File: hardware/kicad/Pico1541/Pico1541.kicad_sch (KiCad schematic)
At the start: 36 parts, among them J1 SWD, J2 USB_A, J3 Micro SD Card, J4 DIN-6, J5 Serial, J6 Display/Keys, J7 OLED/Key_Hat, J8 OLED, J9 5V_EXT, Q1 2N3904, SW1 Reset, SW2 Button1, SW3 Button2, SW4 Button3, SW5 Button4, U1 74LS05, U2 SRV05-4

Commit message: Started PCB layout
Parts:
- removed Q1: 2N3904, Package_TO_SOT_THT:TO-92_Inline, symbol Transistor_BJT:2N3904
- added Q1: MMBT3904, Package_TO_SOT_SMD:SOT-23, symbol Transistor_BJT:MMBT3904
- D2: renamed from D1; footprint LED_THT:LED_D5.0mm-4_RGB -> LED_THT:LED_D5.0mm-4_RGB_Staggered_Pins
- J9: renamed from J4; footprint (none) -> Pico1541-footprints:DIN-6-240deg
- RN1: renamed from RN3; footprint Resistor_SMD:R_Array_Convex_5x1206 -> Resistor_SMD:R_Array_Convex_5x0603
- RN2: renamed from RN4; footprint Resistor_SMD:R_Array_Concave_4x0603 -> Resistor_SMD:R_Array_Convex_4x0603
- RN3: renamed from RN1; footprint Resistor_SMD:R_Array_Concave_4x0603 -> Resistor_SMD:R_Array_Convex_4x0603
- RN4: renamed from RN2; footprint Resistor_SMD:R_Array_Concave_4x0603 -> Resistor_SMD:R_Array_Convex_4x0603
- renumbered C6 to C1, C1 to C2, C10 to C3, C3 to C4, C2 to C5, C4 to C6, C5 to C7, D3 to D1, D2 to D3, J5 to J2, J6 to J3, J3 to J4, J9 to J5, J2 to J6, R2 to R1, R1 to R2, SW4 to SW3, SW3 to SW4
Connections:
- net +3.3V: now also RN2.4 (R4.1); no longer RN2.1 (R1.1)
- net ATN_IEC: now also U1.5; no longer U1.11
- net ATN_RX: now also RN3.8 (R1.2), U1.6; no longer RN3.7 (R2.2), U1.10
- net CLK_IEC: now also U1.11, U1.2; no longer U1.5, U1.8
- net CLK_RX: now also U1.10; no longer U1.6
- net CLK_TX: now also U1.1; no longer U1.9
- net DATA_IEC: now also RN4.8 (R1.2), U1.9; no longer RN4.5 (R4.2), U1.1
- net DATA_RX: now also U1.8; no longer U1.2
- net GND: now also Q1.2 (E)
- net RESET_IEC: now also RN4.5 (R4.2); no longer RN4.8 (R1.2)
- net RESET_RX: now also RN3.7 (R2.2); no longer RN3.8 (R1.2)
- net at A1.31 (GPIO26_ADC0): now also RN2.1 (R1.1); no longer RN2.2 (R2.1)
- net at A1.32 (GPIO27_ADC1): now also RN2.2 (R2.1); no longer RN2.3 (R3.1)
- net at A1.34 (GPIO28_ADC2): now also RN2.3 (R3.1); no longer RN2.4 (R4.1)
- net at RN2.5 (R4.2): now also D3.2 (A); no longer D2.4 (BA)
- net at RN2.6 (R3.2): now also D2.4 (BA); no longer D2.3 (GA)
- net at RN2.7 (R2.2): now also D2.3 (GA); no longer D2.2 (RA)
- net at RN2.8 (R1.2): now also D2.2 (RA); no longer D3.2 (A)
- net at LS1.2, R2.2: now also Q1.3 (C)
- net at R1.2: now also Q1.1 (B)
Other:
- moved on the sheet: D2, D3, RN4, U1A, U1C, U1D, U1E

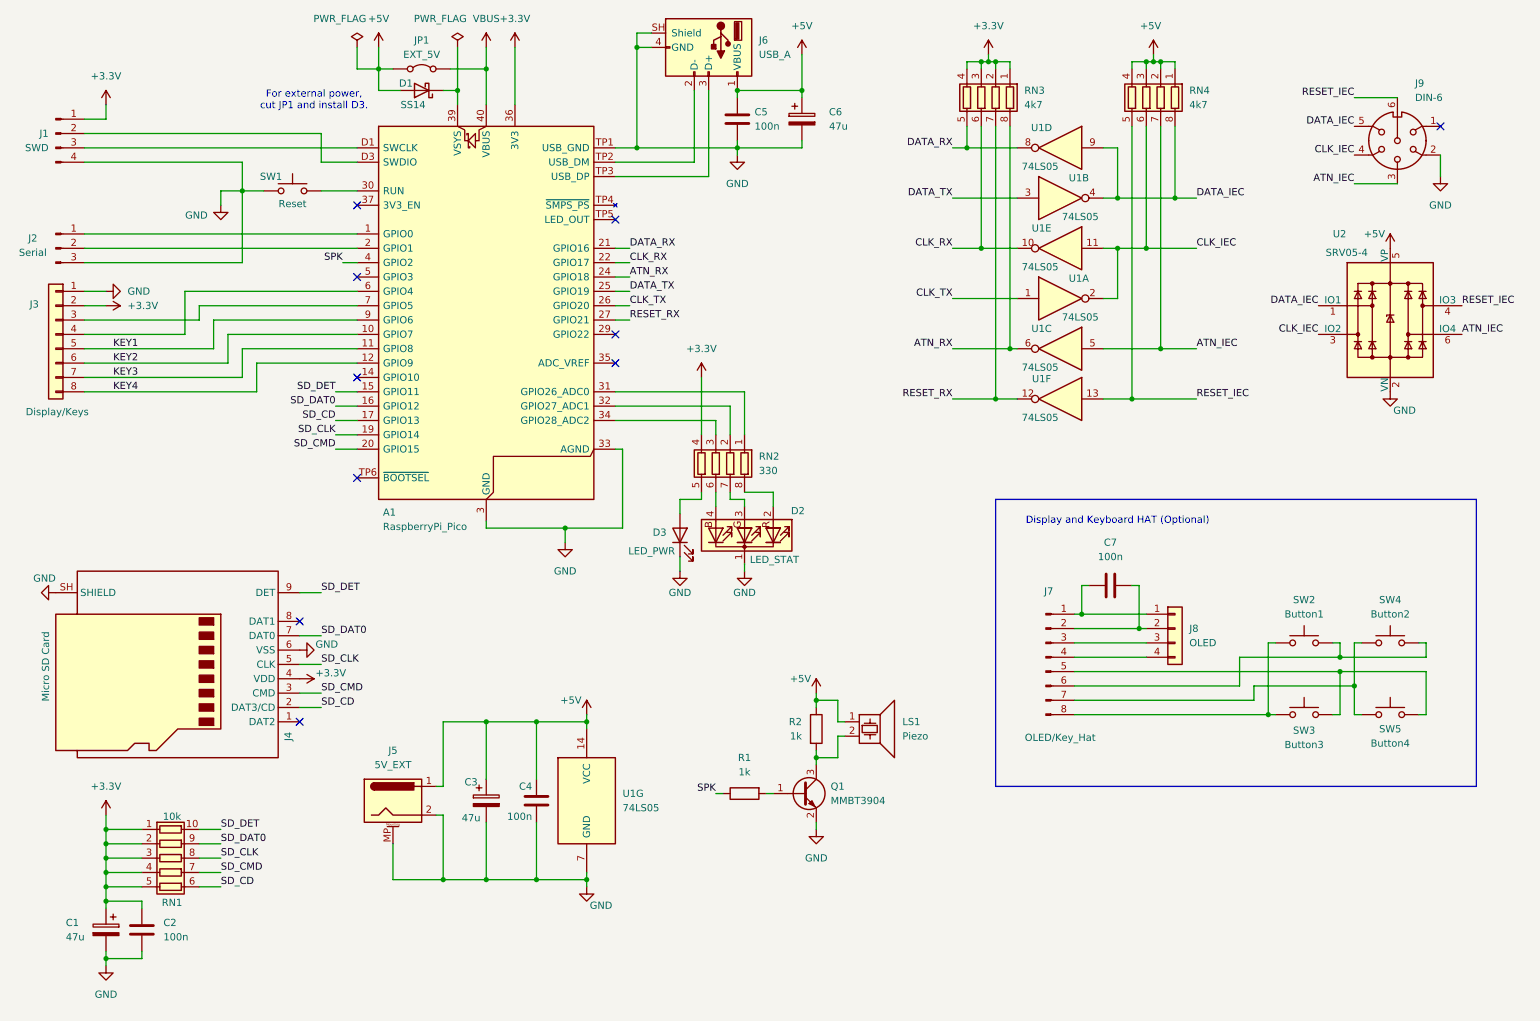
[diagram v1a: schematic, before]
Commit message: Completed PCB design. Still missing break-off tabs.
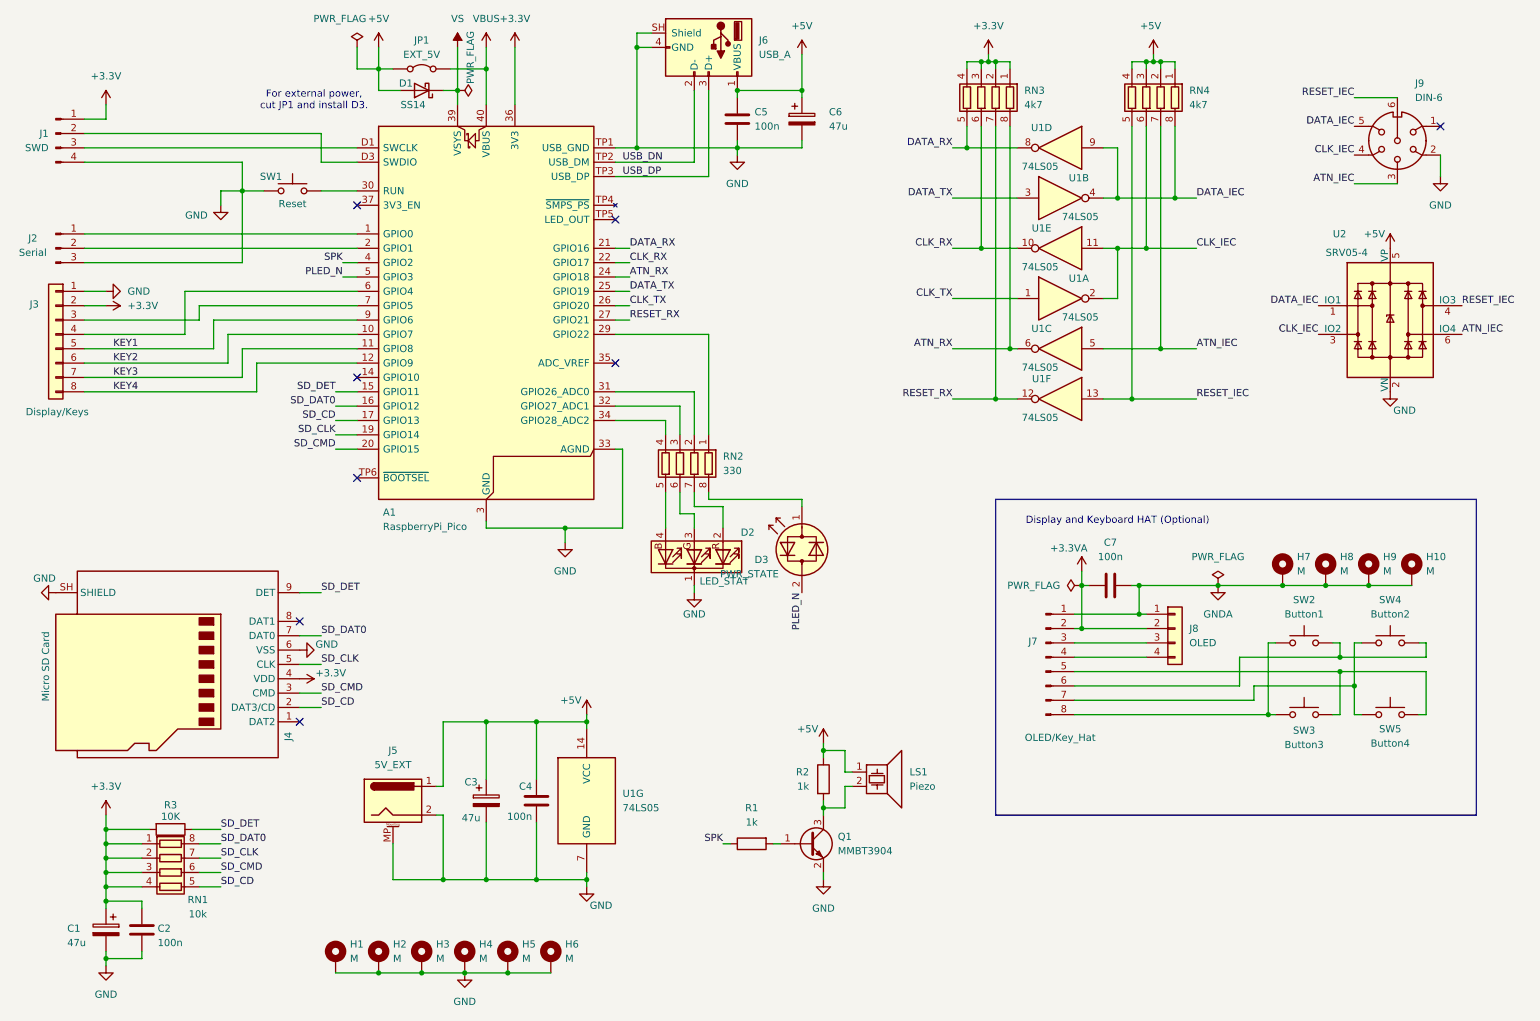
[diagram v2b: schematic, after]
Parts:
- removed D3: LED_PWR, LED_THT:LED_D5.0mm, symbol Device:LED
- removed RN1: 10k, Resistor_SMD:R_Array_Convex_5x0603, symbol Device:R_Pack05
- added D3: PWR_STATE, LED_THT:LED_D5.0mm, symbol Device:LED_Dual_Bidirectional
- added H1, H10, H2, H3, H4, H5, H6, H7, H8, H9: M, MountingHole:MountingHole_2.5mm_Pad_Via, symbol Mechanical:MountingHole_Pad
- added R3: 10K, Resistor_SMD:R_0603_1608Metric_Pad0.98x0.95mm_HandSolder, symbol Device:R
- added RN1: 10k, Resistor_SMD:R_Array_Convex_4x0603, symbol Device:R_Pack04
- U1: footprint Package_SO:SO-14_5.3x10.2mm_P1.27mm -> Package_SO:SO-14_3.9x8.65mm_P1.27mm
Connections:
- net +3.3V: now also R3.2, RN1.1 (R1.1), RN1.2 (R2.1), RN1.3 (R3.1), RN1.4 (R4.1); no longer RN2.4 (R4.1)
- net GND: now also H1.1, H2.1, H3.1, H4.1, H5.1, H6.1
- net SD_CD: now also RN1.5 (R4.2)
- net SD_CLK: now also RN1.7 (R2.2)
- net SD_CMD: now also RN1.6 (R3.2)
- net SD_DAT0: now also RN1.8 (R1.2)
- net SD_DET: now also R3.1
- net at RN2.1 (R1.1): now also A1.29 (GPIO22); no longer A1.31 (GPIO26_ADC0)
- net at RN2.2 (R2.1): now also A1.31 (GPIO26_ADC0); no longer A1.32 (GPIO27_ADC1)
- net at RN2.3 (R3.1): now also A1.32 (GPIO27_ADC1); no longer A1.34 (GPIO28_ADC2)
- net at RN2.5 (R4.2): now also D2.4 (BA)
- net at RN2.6 (R3.2): now also D2.3 (GA); no longer D2.4 (BA)
- net at RN2.7 (R2.2): now also D2.2 (RA); no longer D2.3 (GA)
- net at RN2.8 (R1.2): now also D3.1 (KA); no longer D2.2 (RA)
- net USB_DN: now reaches A1.TP2 (USB_DM), J6.2 (D-)
- net USB_DP: now reaches A1.TP3 (USB_DP), J6.3 (D+)
- net VS: now reaches A1.39 (VSYS), D1.1 (K)
- net PLED_N: now reaches A1.5 (GPIO3)
- net PLED_N: now also D3.2 (AK)
- net GNDA: now reaches J7.1 (Pin_1), J8.1 (Pin_1)
- net GNDA: now also C7.2, H10.1, H7.1, H8.1, H9.1; no longer C7.1
- net +3.3VA: now reaches J7.2 (Pin_2), J8.2 (Pin_2)
- net +3.3VA: now also C7.1; no longer C7.2
- new net: A1.34 (GPIO28_ADC2), RN2.4 (R4.1)
- no-connect marks 10 -> 8
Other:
- moved on the sheet: D2, LS1, Q1, R1, R2, RN2

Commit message: Finalized design.
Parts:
- added FID1, FID2, FID3, FID4, FID5, FID6: Fiducial, Fiducial:Fiducial_1mm_Mask3mm, symbol Mechanical:Fiducial

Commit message: Added support for activity LED.
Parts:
- D2: footprint LED_THT:LED_D5.0mm-4_RGB_Staggered_Pins -> Pico1541-footprints:LED_D5.0mm-4_RGB_CorrectStaggered_Pins
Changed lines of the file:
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@@
 			)
 		)
-		(property "Footprint" "LED_THT:LED_D5.0mm-4_RGB_Staggered_Pins"
+		(property "Footprint" "Pico1541-footprints:LED_D5.0mm-4_RGB_CorrectStaggered_Pins"
 			(at 133.35 111.76 0)
 			(hide yes)

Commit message: fix(pio): set GPIO 10 direction to output and log first 16 bytes of track
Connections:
- net +5V: no longer U2.5 (VP)
- no-connect marks 8 -> 9
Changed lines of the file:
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@@
 	)
 	(no_connect
+		(at 257.81 57.15)
+	)
+	(no_connect
 		(at 74.93 80.01)
 	)
@@
 					(unit 1)
 				)
-			)
-		)
-	)
-	(symbol
-		(lib_id "power:+5V")
-		(at 257.81 57.15 0)
-		(unit 1)
-		(body_style 1)
-		(exclude_from_sim no)
-		(in_bom yes)
-		(on_board yes)
-		(in_pos_files yes)
-		(dnp no)
-		(property "Reference" "#PWR025"
-			(at 257.81 60.96 0)
-			(hide yes)
-			(show_name no)
-			(do_not_autoplace no)
-			(effects
-				(font
-					(size 1.27 1.27)
-				)
-			)
-		)
-		(property "Value" "+5V"
-			(at 255.016 54.61 0)
-			(show_name no)
-			(do_not_autoplace no)
-			(effects
-				(font
-					(size 1.27 1.27)
-				)
-			)
-		)
-		(property "Footprint" ""
-			(at 257.81 57.15 0)
-			(hide yes)
-			(show_name no)
-			(do_not_autoplace no)
-			(effects
-				(font
-					(size 1.27 1.27)
-				)
-			)
-		)
-		(property "Datasheet" ""
-			(at 257.81 57.15 0)
-			(hide yes)
-			(show_name no)
-			(do_not_autoplace no)
-			(effects
-				(font
-					(size 1.27 1.27)
-				)
-			)
-		)
-		(property "Description" "Power symbol creates a global label with name \"+5V\""
-			(at 257.81 57.15 0)
-			(hide yes)
-			(show_name no)
-			(do_not_autoplace no)
-			(effects
-				(font
-					(size 1.27 1.27)
-				)
-			)
-		)
-		(pin "1"
-		)
-		(instances
-			(project "Pico1541"
-				(path "/fb7a9a9a-73a1-4d45-b1f9-1589f10de67b"
-					(reference "#PWR025")
-					(unit 1)
-				)
